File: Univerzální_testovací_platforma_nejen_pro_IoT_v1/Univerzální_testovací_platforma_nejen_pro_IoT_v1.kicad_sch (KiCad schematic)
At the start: 113 parts, among them J1 Conn_01x22_Female ESP S3, J2 Conn_01x22_Female ESPS3, J3 Conn_01x19_Female ESP DEV_KIT, J4 Conn_01x19_Female ESP DEV_KIT, J5 Conn_02x03_Counter_Clockwise, J6 USB_C_Receptacle, SW1 SW_Push, U1 STM32F103ZETx, U2 AMS1117CS-3.3, Y1 12Mhz

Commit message: průběžná commit
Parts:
- removed C16: 1uF, Capacitor_SMD:C_0603_1608Metric_Pad1.08x0.95mm_HandSolder, symbol Device:C
- removed FB1: 120R, symbol Device:FerriteBead
- removed SW1: SW_Push, symbol Switch:SW_Push
- added J7, J8: Conn_02x10_Odd_Even, Connector_PinHeader_2.54mm:PinHeader_2x10_P2.54mm_Vertical, symbol Connector_Generic:Conn_02x10_Odd_Even
- added SW1: SW_Push_Dual, Button_Switch_SMD:SW_SPST_TL3342, symbol Switch:SW_Push_Dual
- C1, C2, C3, C4: footprint (none) -> Capacitor_SMD:C_0402_1005Metric_Pad0.74x0.62mm_HandSolder; LCSC (none) -> C307331
- C10, C11, C14, C9: footprint (none) -> Capacitor_SMD:C_0805_2012Metric_Pad1.18x1.45mm_HandSolder; LCSC (none) -> C49678
- C18: footprint (none) -> Capacitor_Tantalum_SMD:CP_EIA-6032-20_AVX-F_Pad2.25x2.35mm_HandSolder; LCSC (none) -> C2798049
- C19, C20: footprint (none) -> Capacitor_SMD:C_0603_1608Metric_Pad1.08x0.95mm_HandSolder; LCSC (none) -> C1647
- C5, C6, C7, C8: footprint (none) -> Capacitor_SMD:C_0603_1608Metric_Pad1.08x0.95mm_HandSolder; LCSC (none) -> C14663
- J1: footprint (none) -> Connector_PinHeader_2.54mm:PinHeader_1x22_P2.54mm_Vertical; LCSC (none) -> C2886702
- J2: value Conn_01x22_Female ESPS3 -> Conn_01x22_Female ESP S3; footprint (none) -> Connector_PinHeader_2.54mm:PinHeader_1x22_P2.54mm_Vertical; LCSC (none) -> C2886702
- J3, J4: footprint (none) -> Connector_PinHeader_2.54mm:PinHeader_1x19_P2.54mm_Vertical; LCSC (none) -> C319202
- J5: footprint (none) -> Connector_PinHeader_2.54mm:PinHeader_2x03_P2.54mm_Vertical; LCSC (none) -> C2894964
- J6: footprint (none) -> Connector_USB:USB_C_Receptacle_XKB_U262-16XN-4BVC11
- JP1: footprint (none) -> Connector_PinHeader_2.54mm:PinHeader_1x02_P2.54mm_Vertical; LCSC (none) -> C2905434
- U1: LCSC (none) -> C8287
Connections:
- net GND: now also SW1.1
- net OSC_IN: no longer C19.1, U1.24 (RCC_OSC_OUT), Y1.1
- net at C15.1, R2.2, U1.25 (NRST): now also SW1.2
- net at U1.100 (PA8): now also J7.17 (Pin_17)
- net at U1.101 (PA9): now also J7.19 (Pin_19)
- net PA10: now reaches U1.102 (PA10)
- net PA10: now also J7.2 (Pin_2)
- net PA13: now reaches U1.105 (PA13)
- net PA13: now also J7.4 (Pin_4)
- net PA14: now reaches U1.109 (PA14)
- net PA14: now also J7.6 (Pin_6)
- net PA15: now reaches U1.110 (PA15)
- net PA15: now also J7.8 (Pin_8)
- net PF3: now reaches U1.13 (PF3)
- net PF3: now also J8.19 (Pin_19)
- net PF4: now reaches U1.14 (PF4)
- net PF4: now also J8.2 (Pin_2)
- net PF5: now reaches U1.15 (PF5)
- net PF5: now also J8.4 (Pin_4)
- net PF6: now reaches U1.18 (PF6)
- net PF6: now also J8.6 (Pin_6)
- net PF7: now reaches U1.19 (PF7)
- net PF7: now also J8.8 (Pin_8)
- net PF8: now reaches U1.20 (PF8)
- net PF8: now also J8.10 (Pin_10)
- net PF9: now reaches U1.21 (PF9)
- net PF9: now also J8.12 (Pin_12)
- net PF10: now reaches U1.22 (PF10)
- net PF10: now also J8.14 (Pin_14)
- net at U1.34 (PA0): now also J7.1 (Pin_1)
- net at U1.35 (PA1): now also J7.3 (Pin_3)
- net at U1.36 (PA2): now also J7.5 (Pin_5)
- net at U1.37 (PA3): now also J7.7 (Pin_7)
- net at U1.40 (PA4): now also J7.9 (Pin_9)
- net at U1.41 (PA5): now also J7.11 (Pin_11)
- net at U1.42 (PA6): now also J7.13 (Pin_13)
- net at U1.43 (PA7): now also J7.15 (Pin_15)
- net PC4: now reaches U1.44 (PC4)
- net PC4: now also J7.14 (Pin_14)
- net PC5: now reaches U1.45 (PC5)
- net PC5: now also J7.16 (Pin_16)
- net PB0: now reaches U1.46 (PB0)
- net PB0: now also J7.10 (Pin_10)
- net PB1: now reaches U1.47 (PB1)
- net PB1: now also J7.12 (Pin_12)
- net PF11: now reaches U1.49 (PF11)
- net PF11: now also J8.16 (Pin_16)
- net PF12: now reaches U1.50 (PF12)
- net PF12: now also J8.18 (Pin_18)
- net PE14: now reaches U1.67 (PE14)
- net PE14: now also J8.15 (Pin_15)
- net PE15: now reaches U1.68 (PE15)
- net PE15: now also J8.17 (Pin_17)
- net PD9: now reaches U1.78 (PD9)
- net PD9: now also J8.3 (Pin_3)
- net PD10: now reaches U1.79 (PD10)
- net PD10: now also J8.5 (Pin_5)
- net PD11: now reaches U1.80 (PD11)
- net PD11: now also J8.7 (Pin_7)
- net PD12: now reaches U1.81 (PD12)
- net PD12: now also J8.9 (Pin_9)
- net PD13: now reaches U1.82 (PD13)
- net PD13: now also J8.11 (Pin_11)
- net PD14: now reaches U1.85 (PD14)
- net PD14: now also J8.13 (Pin_13)
- net PC6: now reaches U1.96 (PC6)
- net PC6: now also J7.18 (Pin_18)
- net PC7: now reaches U1.97 (PC7)
- net PC7: now also J7.20 (Pin_20)
- net PC8: now reaches U1.98 (PC8)
- net PC8: now also J8.1 (Pin_1)
- new net OSC_OUT: C19.1, U1.24 (RCC_OSC_OUT), Y1.1
- no-connect marks 11 -> 17
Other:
- note added: "Crystal oscilator"
- note added: "Power supply"
- note removed: "Crystal"
- note removed: "Power supply, which one???"
- moved on the sheet: C13, C14, J4, JP1, R22, R23, R24, R25, R26, R27, R28, R29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

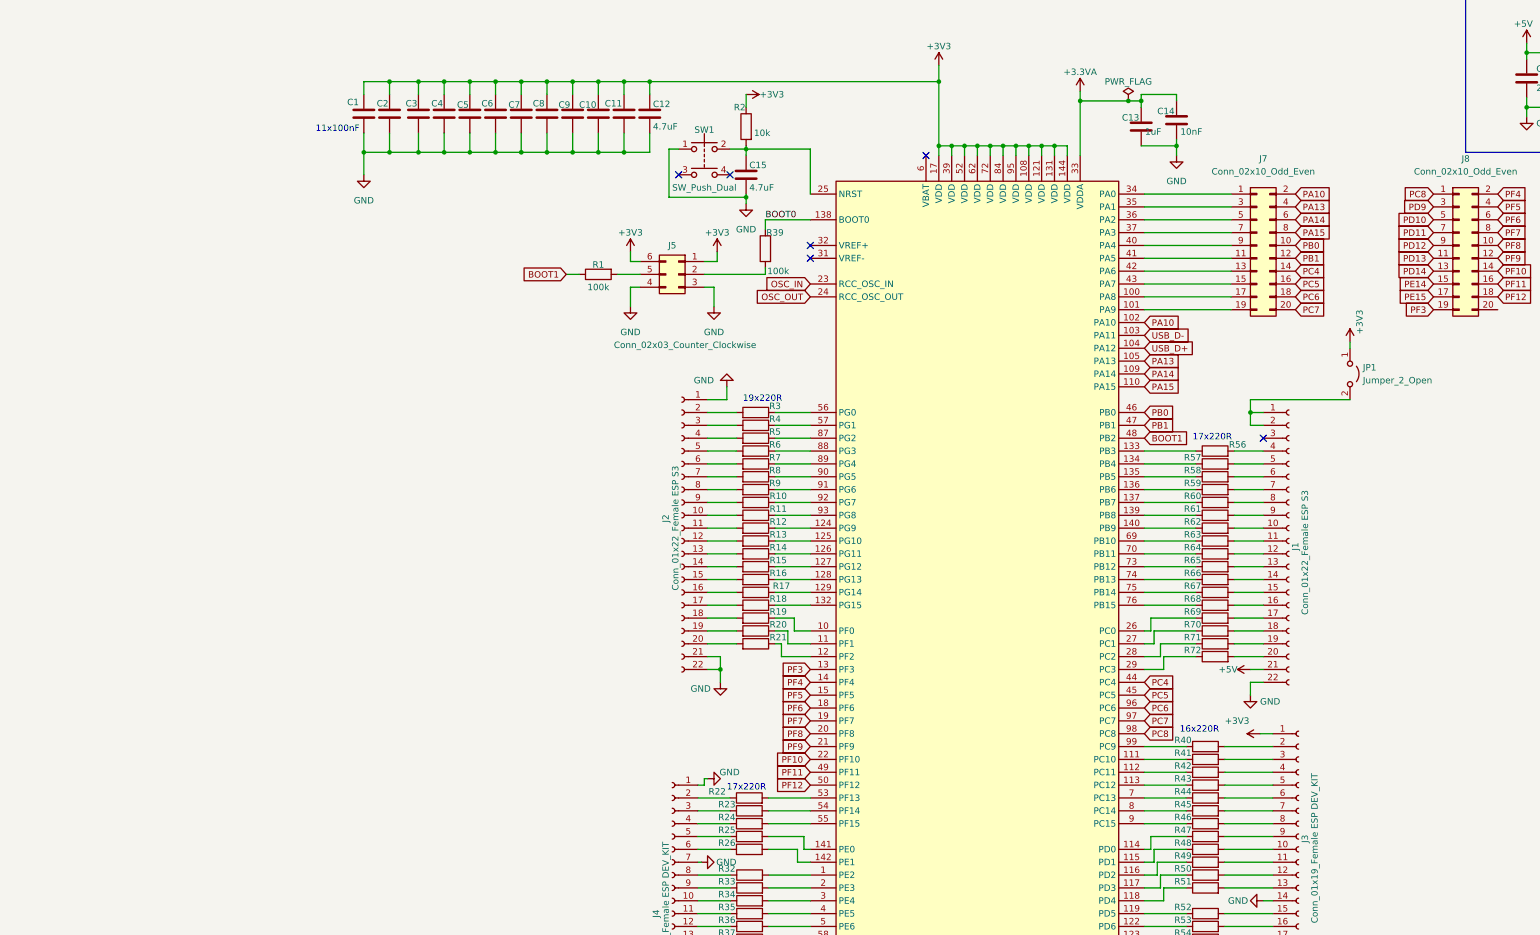
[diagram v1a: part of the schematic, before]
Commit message: začátek hierarchických sheetů
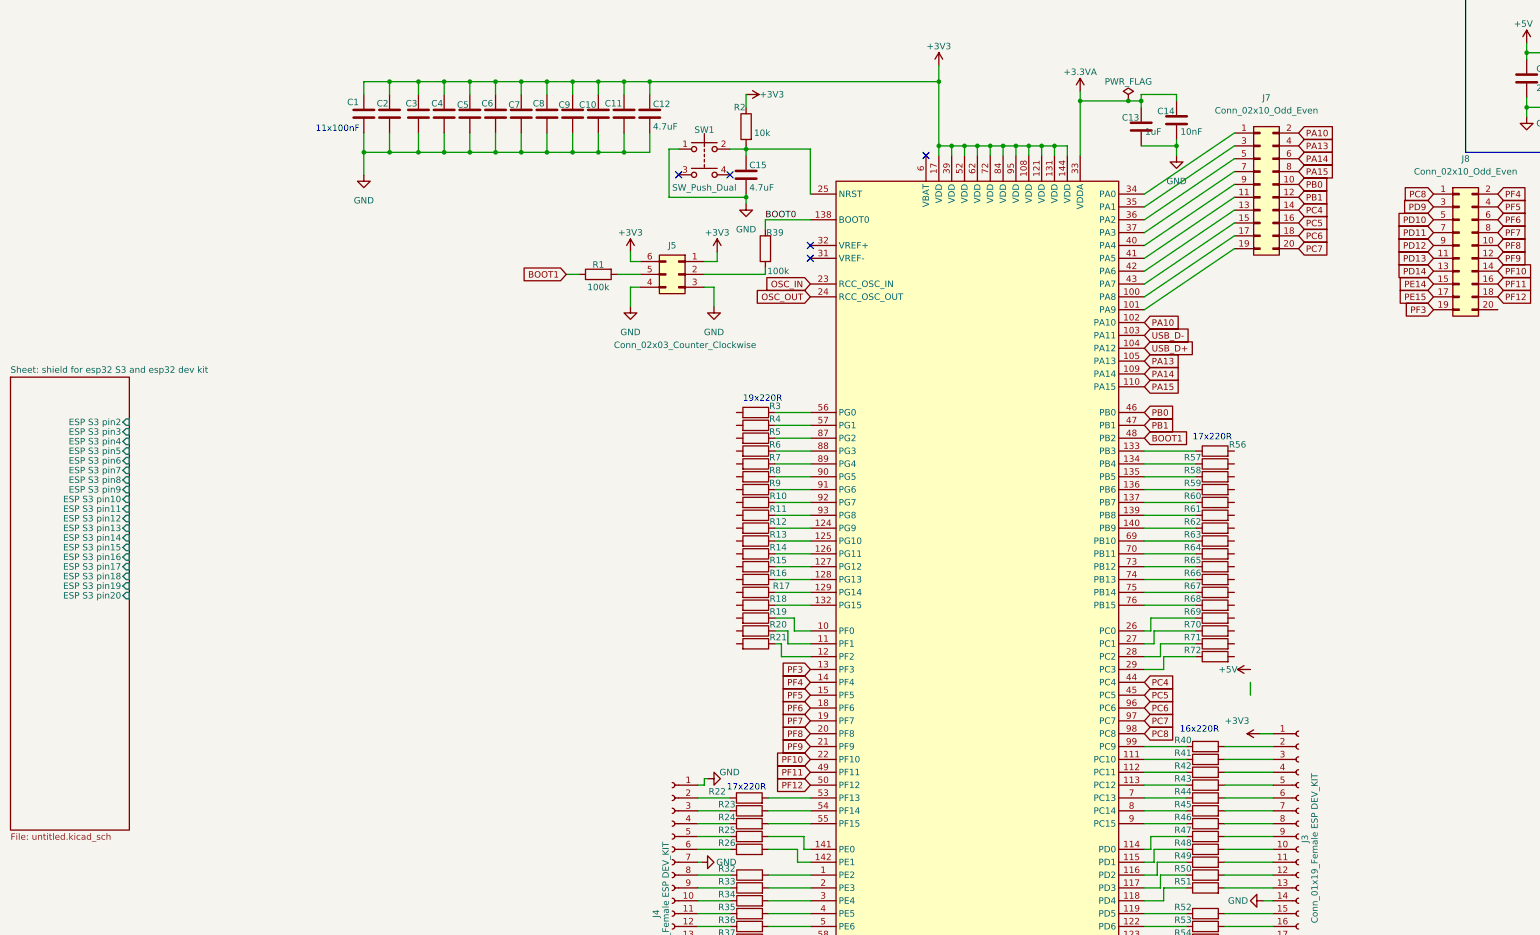
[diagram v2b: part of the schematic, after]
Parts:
- removed J1, J2: Conn_01x22_Female ESP S3, Connector_PinHeader_2.54mm:PinHeader_1x22_P2.54mm_Vertical, symbol Connector:Conn_01x22_Female
- removed JP1: Jumper_2_Open, Connector_PinHeader_2.54mm:PinHeader_1x02_P2.54mm_Vertical, symbol Jumper:Jumper_2_Open
- J3, J4: footprint Connector_PinHeader_2.54mm:PinHeader_1x19_P2.54mm_Vertical -> Connector_PinSocket_2.54mm:PinSocket_1x19_P2.54mm_Vertical
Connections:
- no-connect marks 17 -> 16
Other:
- added sheet Sheet: shield for esp32 S3 and esp32 dev kit (untitled.kicad_sch)
- moved on the sheet: J7
